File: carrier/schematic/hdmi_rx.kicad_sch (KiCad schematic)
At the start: 7 parts, among them J901 HDMI-019S, U901 M24C02-WMN6TP

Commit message: carrier: wave-2 consolidated regeneration — ALL round-4 gates live (POWER TREE 12 regulators / TESTPOINTS 43+9 / SPICE 14 checks incl. the caught CP2102N abs-max fix), LINK 0/0, goldens 23/23, byte-deterministic
Co-Authored-By: Claude Fable 5 <noreply@anthropic.com>
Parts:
- J901: MPN (none) -> HDMI-019S
- U901: MPN (none) -> M24C02-WMN6TP
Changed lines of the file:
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@@
 		(property
 			"Datasheet"
-			""
+			"https://www.lcsc.com/datasheet/C7562.pdf"
 			(at 113.03 64.77 0)
 			(effects
@@
 			)
 		)
+		(property
+			"MPN"
+			"M24C02-WMN6TP"
+			(at 113.03 64.77 0)
+			(effects
+				(font
+					(size 1.27 1.27)
+				)
+				(hide yes)
+			)
+		)
 		(pin
 			"1"
@@
 				"Zynq_Carrier"
 				(path
-					"/210e47c2-a83b-45be-ae0a-d7b3f3834bfa/3d16c4d5-210e-462e-b61d-a9f0fecc8e09"
+					"/c2797150-7a6e-556a-82f5-fdda13c31368/1e15c56c-3a37-58d2-aa9b-64efface14d2"
 					(reference "U901")
 					(unit 1)
@@
 		(property
 			"Datasheet"
-			""
+			"https://www.lcsc.com/datasheet/C111617.pdf"
 			(at 185.42 90.17 0)
 			(effects
@@
 			)
 		)
+		(property
+			"MPN"
+			"HDMI-019S"
+			(at 185.42 90.17 0)
+			(effects
+				(font
+					(size 1.27 1.27)
+				)
+				(hide yes)
+			)
+		)
 		(pin
 			"16"
@@
 				"Zynq_Carrier"
 				(path
-					"/210e47c2-a83b-45be-ae0a-d7b3f3834bfa/3d16c4d5-210e-462e-b61d-a9f0fecc8e09"
+					"/c2797150-7a6e-556a-82f5-fdda13c31368/1e15c56c-3a37-58d2-aa9b-64efface14d2"
 					(reference "J901")
 					(unit 1)
@@
 				"Zynq_Carrier"
 				(path
-					"/210e47c2-a83b-45be-ae0a-d7b3f3834bfa/3d16c4d5-210e-462e-b61d-a9f0fecc8e09"
+					"/c2797150-7a6e-556a-82f5-fdda13c31368/1e15c56c-3a37-58d2-aa9b-64efface14d2"
 					(reference "R902")
 					(unit 1)
@@
 				"Zynq_Carrier"
 				(path
-					"/210e47c2-a83b-45be-ae0a-d7b3f3834bfa/3d16c4d5-210e-462e-b61d-a9f0fecc8e09"
+					"/c2797150-7a6e-556a-82f5-fdda13c31368/1e15c56c-3a37-58d2-aa9b-64efface14d2"
 					(reference "R901")
 					(unit 1)
@@
 				"Zynq_Carrier"
 				(path
-					"/210e47c2-a83b-45be-ae0a-d7b3f3834bfa/3d16c4d5-210e-462e-b61d-a9f0fecc8e09"
+					"/c2797150-7a6e-556a-82f5-fdda13c31368/1e15c56c-3a37-58d2-aa9b-64efface14d2"
 					(reference "R903")
 					(unit 1)
@@
 				"Zynq_Carrier"
 				(path
-					"/210e47c2-a83b-45be-ae0a-d7b3f3834bfa/3d16c4d5-210e-462e-b61d-a9f0fecc8e09"
+					"/c2797150-7a6e-556a-82f5-fdda13c31368/1e15c56c-3a37-58d2-aa9b-64efface14d2"
 					(reference "R904")
 					(unit 1)
@@
 				"Zynq_Carrier"
 				(path
-					"/210e47c2-a83b-45be-ae0a-d7b3f3834bfa/3d16c4d5-210e-462e-b61d-a9f0fecc8e09"
+					"/c2797150-7a6e-556a-82f5-fdda13c31368/1e15c56c-3a37-58d2-aa9b-64efface14d2"
 					(reference "C901")
 					(unit 1)
@@
 				"Zynq_Carrier"
 				(path
-					"/210e47c2-a83b-45be-ae0a-d7b3f3834bfa/3d16c4d5-210e-462e-b61d-a9f0fecc8e09"
+					"/c2797150-7a6e-556a-82f5-fdda13c31368/1e15c56c-3a37-58d2-aa9b-64efface14d2"
 					(reference "#PWR901")
 					(unit 1)
@@
 				"Zynq_Carrier"
 				(path
-					"/210e47c2-a83b-45be-ae0a-d7b3f3834bfa/3d16c4d5-210e-462e-b61d-a9f0fecc8e09"
+					"/c2797150-7a6e-556a-82f5-fdda13c31368/1e15c56c-3a37-58d2-aa9b-64efface14d2"
 					(reference "#PWR902")
 					(unit 1)
@@
 				"Zynq_Carrier"
 				(path
-					"/210e47c2-a83b-45be-ae0a-d7b3f3834bfa/3d16c4d5-210e-462e-b61d-a9f0fecc8e09"
+					"/c2797150-7a6e-556a-82f5-fdda13c31368/1e15c56c-3a37-58d2-aa9b-64efface14d2"
 					(reference "#PWR903")
 					(unit 1)
@@
 				"Zynq_Carrier"
 				(path
-					"/210e47c2-a83b-45be-ae0a-d7b3f3834bfa/3d16c4d5-210e-462e-b61d-a9f0fecc8e09"
+					"/c2797150-7a6e-556a-82f5-fdda13c31368/1e15c56c-3a37-58d2-aa9b-64efface14d2"
 					(reference "#PWR904")
 					(unit 1)
@@
 				"Zynq_Carrier"
 				(path
-					"/210e47c2-a83b-45be-ae0a-d7b3f3834bfa/3d16c4d5-210e-462e-b61d-a9f0fecc8e09"
+					"/c2797150-7a6e-556a-82f5-fdda13c31368/1e15c56c-3a37-58d2-aa9b-64efface14d2"
 					(reference "#PWR905")
 					(unit 1)
@@
 				"Zynq_Carrier"
 				(path
-					"/210e47c2-a83b-45be-ae0a-d7b3f3834bfa/3d16c4d5-210e-462e-b61d-a9f0fecc8e09"
+					"/c2797150-7a6e-556a-82f5-fdda13c31368/1e15c56c-3a37-58d2-aa9b-64efface14d2"
 					(reference "#PWR906")
 					(unit 1)
@@
 				"Zynq_Carrier"
 				(path
-					"/210e47c2-a83b-45be-ae0a-d7b3f3834bfa/3d16c4d5-210e-462e-b61d-a9f0fecc8e09"
+					"/c2797150-7a6e-556a-82f5-fdda13c31368/1e15c56c-3a37-58d2-aa9b-64efface14d2"
 					(reference "#PWR907")
 					(unit 1)
@@
 				"Zynq_Carrier"
 				(path
-					"/210e47c2-a83b-45be-ae0a-d7b3f3834bfa/3d16c4d5-210e-462e-b61d-a9f0fecc8e09"
+					"/c2797150-7a6e-556a-82f5-fdda13c31368/1e15c56c-3a37-58d2-aa9b-64efface14d2"
 					(reference "#PWR908")
 					(unit 1)
@@
 				"Zynq_Carrier"
 				(path
-					"/210e47c2-a83b-45be-ae0a-d7b3f3834bfa/3d16c4d5-210e-462e-b61d-a9f0fecc8e09"
+					"/c2797150-7a6e-556a-82f5-fdda13c31368/1e15c56c-3a37-58d2-aa9b-64efface14d2"
 					(reference "#FLG901")
 					(unit 1)

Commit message: audit-fix(engine): harvest F1-F7,F9 — gate hardening + leak + guards
F1 selftest now exercises the VISUAL gate against geometry mutants (wire-cross
+ text-over-wire) — proven to bite (was never run on a mutant before).
F2 visual_gate catches different-net wire T-touch / butt-join shorts.
F3 netlist_gate no longer leaks tmp .net files (was 2671 stale).
F4 board uniquify guards the stride (widened 100->1000) against ref collision.
F5 hier-mode sheets now re-run through the per-sheet netlist gate.
F6 dead clause dropped; F7 stale zynq_eda docstring fixed; F9 eager inline-pin
validation. Source copied verbatim from the audit-fix worktree (6 files, proven
untouched on origin since its base); board regenerated fresh. All gates green,
selftest geo-mutants killed by the visual gate, goldens 23/23, m1_rc PASS.

Co-Authored-By: Claude Fable 5 <noreply@anthropic.com>
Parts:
- renumbered C901 to C9001, J901 to J9001, R901 to R9001, R902 to R9002, R903 to R9003, R904 to R9004, U901 to U9001
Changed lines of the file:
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@@
 		(property
 			"Reference"
-			"U901"
+			"U9001"
 			(at 118.11 57.785 0)
 			(effects
@@
 				(path
 					"/c2797150-7a6e-556a-82f5-fdda13c31368/1e15c56c-3a37-58d2-aa9b-64efface14d2"
-					(reference "U901")
+					(reference "U9001")
 					(unit 1)
 				)
@@
 		(property
 			"Reference"
-			"J901"
+			"J9001"
 			(at 200.66 57.785 0)
 			(effects
@@
 				(path
 					"/c2797150-7a6e-556a-82f5-fdda13c31368/1e15c56c-3a37-58d2-aa9b-64efface14d2"
-					(reference "J901")
+					(reference "J9001")
 					(unit 1)
 				)
@@
 		(property
 			"Reference"
-			"R902"
+			"R9002"
 			(at 218.543 128.27 0)
 			(effects
@@
 				(path
 					"/c2797150-7a6e-556a-82f5-fdda13c31368/1e15c56c-3a37-58d2-aa9b-64efface14d2"
-					(reference "R902")
+					(reference "R9002")
 					(unit 1)
 				)
@@
 		(property
 			"Reference"
-			"R901"
+			"R9001"
 			(at 92.608 135.89 0)
 			(effects
@@
 				(path
 					"/c2797150-7a6e-556a-82f5-fdda13c31368/1e15c56c-3a37-58d2-aa9b-64efface14d2"
-					(reference "R901")
+					(reference "R9001")
 					(unit 1)
 				)
@@
 		(property
 			"Reference"
-			"R903"
+			"R9003"
 			(at 87.733 54.61 0)
 			(effects
@@
 				(path
 					"/c2797150-7a6e-556a-82f5-fdda13c31368/1e15c56c-3a37-58d2-aa9b-64efface14d2"
-					(reference "R903")
+					(reference "R9003")
 					(unit 1)
 				)
@@
 		(property
 			"Reference"
-			"R904"
+			"R9004"
 			(at 87.733 62.23 0)
 			(effects
@@
 				(path
 					"/c2797150-7a6e-556a-82f5-fdda13c31368/1e15c56c-3a37-58d2-aa9b-64efface14d2"
-					(reference "R904")
+					(reference "R9004")
 					(unit 1)
 				)
@@
 		(property
 			"Reference"
-			"C901"
+			"C9001"
 			(at 211.939 54.61 0)
 			(effects
@@
 				(path
 					"/c2797150-7a6e-556a-82f5-fdda13c31368/1e15c56c-3a37-58d2-aa9b-64efface14d2"
-					(reference "C901")
+					(reference "C9001")
 					(unit 1)
 				)
@@
 		(property
 			"Reference"
-			"#PWR901"
+			"#PWR9001"
 			(at 99.06 64.77 0)
 			(effects
@@
 				(path
 					"/c2797150-7a6e-556a-82f5-fdda13c31368/1e15c56c-3a37-58d2-aa9b-64efface14d2"
-					(reference "#PWR901")
+					(reference "#PWR9001")
 					(unit 1)
 				)
@@
 		(property
 			"Reference"
-			"#PWR902"
+			"#PWR9002"
 			(at 127 69.85 0)
 			(effects
@@
 				(path
 					"/c2797150-7a6e-556a-82f5-fdda13c31368/1e15c56c-3a37-58d2-aa9b-64efface14d2"
-					(reference "#PWR902")
+					(reference "#PWR9002")
 					(unit 1)
 				)
@@
 		(property
 			"Reference"
-			"#PWR903"
+			"#PWR9003"
 			(at 113.03 72.39 0)
 			(effects
@@
 				(path
 					"/c2797150-7a6e-556a-82f5-fdda13c31368/1e15c56c-3a37-58d2-aa9b-64efface14d2"
-					(reference "#PWR903")
+					(reference "#PWR9003")
 					(unit 1)
 				)
@@
 		(property
 			"Reference"
-			"#PWR904"
+			"#PWR9004"
 			(at 193.04 123.19 0)
 			(effects
@@
 				(path
 					"/c2797150-7a6e-556a-82f5-fdda13c31368/1e15c56c-3a37-58d2-aa9b-64efface14d2"
-					(reference "#PWR904")
+					(reference "#PWR9004")
 					(unit 1)
 				)
@@
 		(property
 			"Reference"
-			"#PWR905"
+			"#PWR9005"
 			(at 205.74 123.19 0)
 			(effects
@@
 				(path
 					"/c2797150-7a6e-556a-82f5-fdda13c31368/1e15c56c-3a37-58d2-aa9b-64efface14d2"
-					(reference "#PWR905")
+					(reference "#PWR9005")
 					(unit 1)
 				)
@@
 		(property
 			"Reference"
-			"#PWR906"
+			"#PWR9006"
 			(at 215.9 123.19 0)
 			(effects
@@
 				(path
 					"/c2797150-7a6e-556a-82f5-fdda13c31368/1e15c56c-3a37-58d2-aa9b-64efface14d2"
-					(reference "#PWR906")
+					(reference "#PWR9006")
 					(unit 1)
 				)
@@
 		(property
 			"Reference"
-			"#PWR907"
+			"#PWR9007"
 			(at 85.09 67.31 0)
 			(effects
@@
 				(path
 					"/c2797150-7a6e-556a-82f5-fdda13c31368/1e15c56c-3a37-58d2-aa9b-64efface14d2"
-					(reference "#PWR907")
+					(reference "#PWR9007")
 					(unit 1)
 				)
@@
 		(property
 			"Reference"
-			"#PWR908"
+			"#PWR9008"
 			(at 208.28 57.15 0)
 			(effects
@@
 				(path
 					"/c2797150-7a6e-556a-82f5-fdda13c31368/1e15c56c-3a37-58d2-aa9b-64efface14d2"
-					(reference "#PWR908")
+					(reference "#PWR9008")
 					(unit 1)
 				)
@@
 		(property
 			"Reference"
-			"#FLG901"
+			"#FLG9001"
 			(at 151.13 46.99 0)
 			(effects
@@
 				(path
 					"/c2797150-7a6e-556a-82f5-fdda13c31368/1e15c56c-3a37-58d2-aa9b-64efface14d2"
-					(reference "#FLG901")
-					(unit 1)
-				)
+					(reference "#FLG9001")
+					(unit 1)
+				)

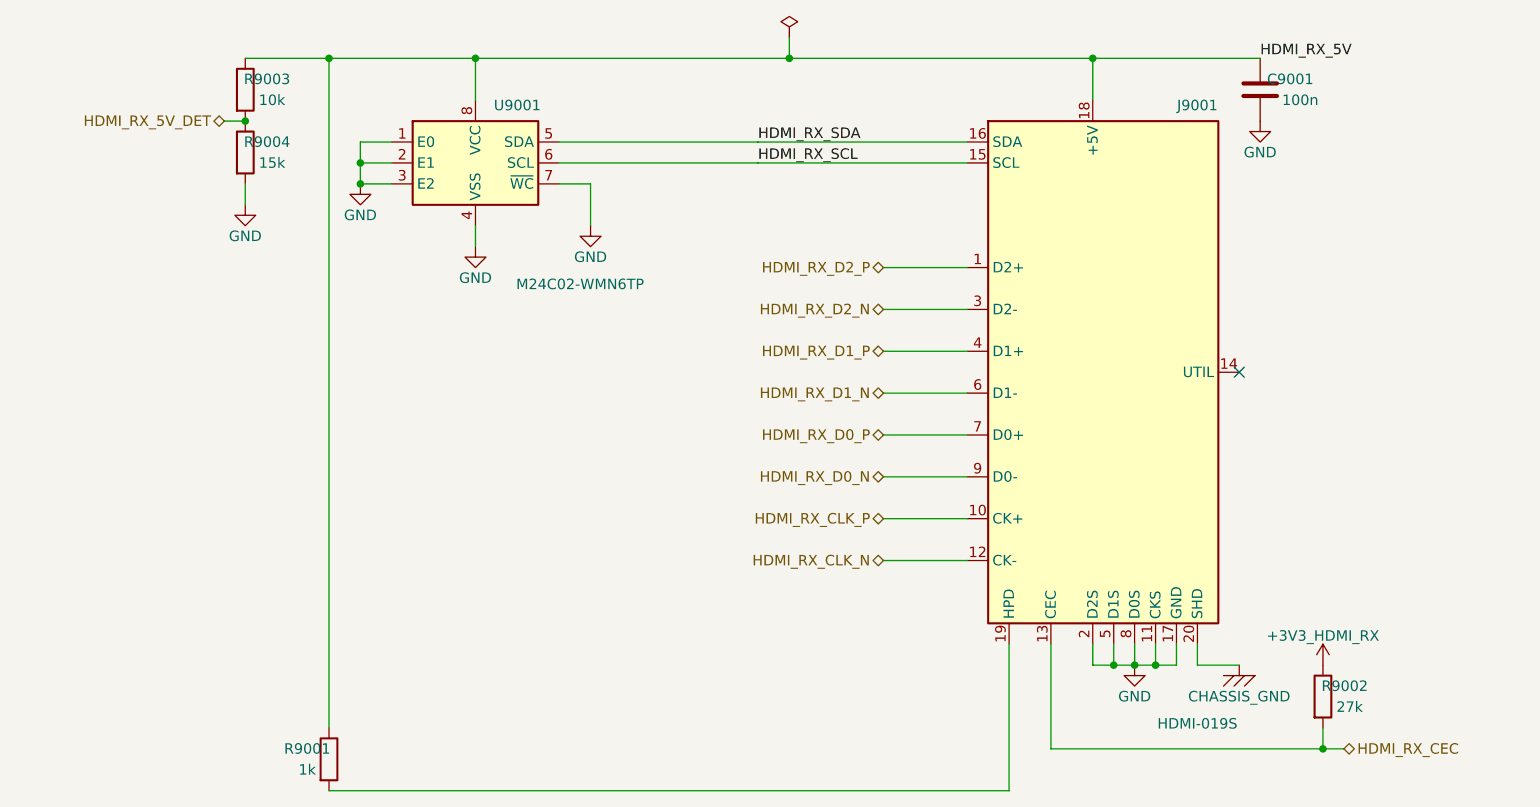
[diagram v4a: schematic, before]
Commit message: carrier: consolidated regen for round-6 audit fixes + PLAN RESOLVED
schgen board regen after SD-1 / HDMIRX-1 / HDMIRX-2 / LCD-1: 23 sheets, all
gates green (board-link, ERC=0, power-tree 16 regs/0 findings, testpoints,
SPICE 21 checks, visual). Goldens drift only on the 3 touched sheets
(microsd/hdmi_rx/lcd schematic+render), BOM (microsd:C4 100n, hdmi_rx:R5 10k,
lcd:C2 2.2u/C125847), reports, floorplan. PLAN findings marked RESOLVED
(HDMIRX-1 = documented verified-part DNP). selftest 44/44 + byte-deterministic.

Co-Authored-By: Claude Fable 5 <noreply@anthropic.com>
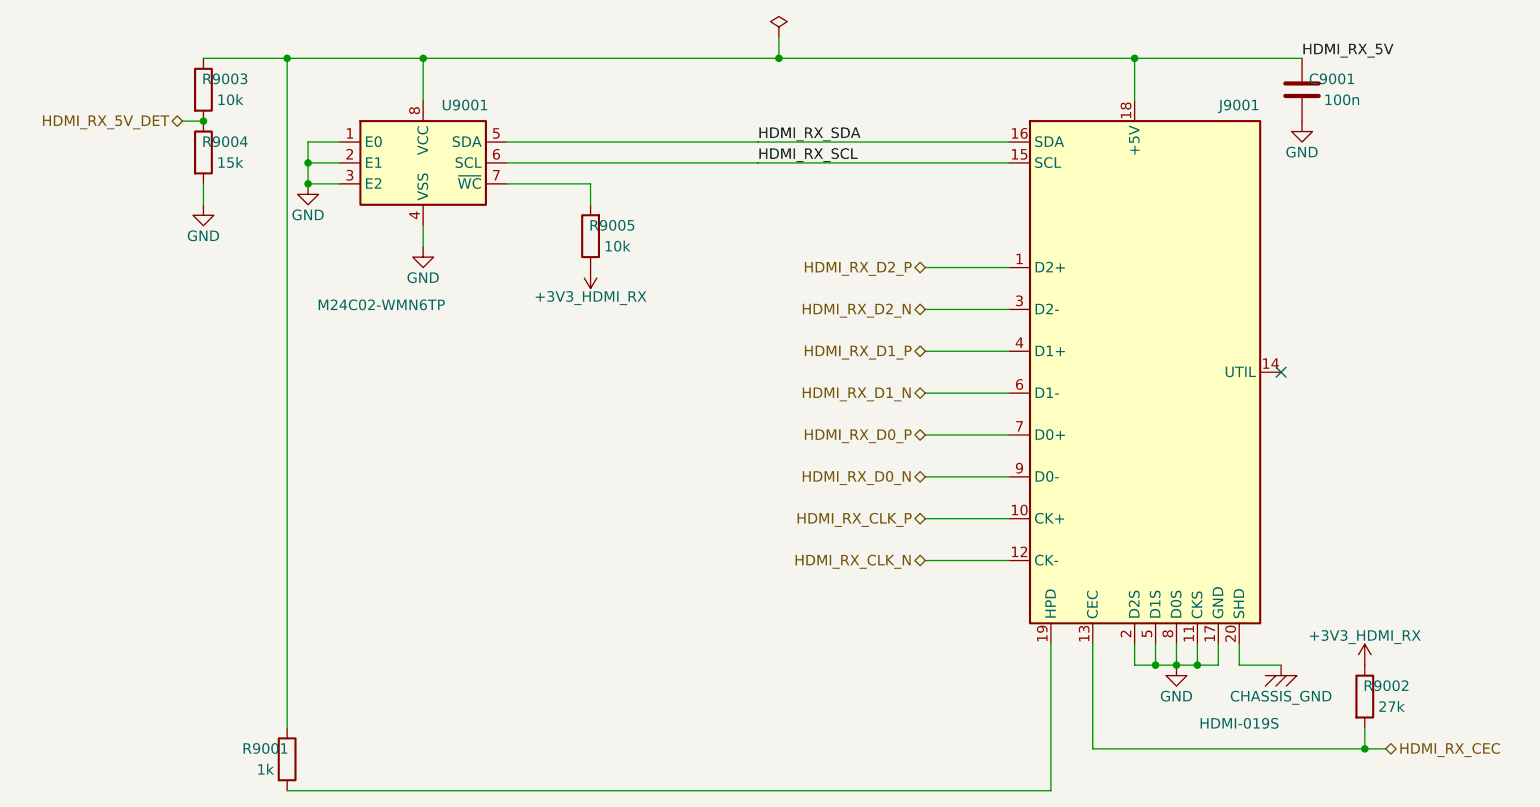
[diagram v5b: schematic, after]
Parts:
- added C9001: 100n, Capacitor_SMD:C_0603_1608Metric, symbol Device:C
- J9001: renamed from R9002; value 27k -> HDMI-019S; footprint Resistor_SMD:R_0603_1608Metric -> HDMI-019S:HDMI-019S; symbol Device:R -> schgen:HDMI_A_RX; LCSC C22967 -> C111617; MPN (none) -> HDMI-019S
- R9001: renamed from R9003; value 10k -> 1k; LCSC C25804 -> C21190
- R9002: renamed from R9001; value 1k -> 27k; LCSC C21190 -> C22967
- R9003: renamed from R9004; value 15k -> 10k; LCSC C22809 -> C25804
- R9004: renamed from C9001; value 100n -> 15k; footprint Capacitor_SMD:C_0603_1608Metric -> Resistor_SMD:R_0603_1608Metric; symbol Device:C -> Device:R; LCSC C14663 -> C22809
- R9005: renamed from J9001; value HDMI-019S -> 10k; footprint HDMI-019S:HDMI-019S -> Resistor_SMD:R_0603_1608Metric; symbol schgen:HDMI_A_RX -> Device:R; LCSC C111617 -> C25804; MPN HDMI-019S -> (none)
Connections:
- net +3V3_HDMI_RX: now also R9002.1, R9005.1; no longer J9001.1
- net CHASSIS_GND: now also J9001.20 (SHD), J9001.21 (SHD), J9001.22 (SHD), J9001.23 (SHD); no longer R9005.20 (SHD), R9005.21 (SHD), R9005.22 (SHD), R9005.23 (SHD)
- net GND: now also J9001.11 (CKS), J9001.17 (GND), J9001.2 (D2S), J9001.5 (D1S), J9001.8 (D0S), C9001.2; no longer R9003.2, R9005.11 (CKS), R9005.17 (GND), R9005.2 (D2S), R9005.5 (D1S), R9005.8 (D0S), U9001.7 (~{WC})
- net HDMI_RX_5V: now also J9001.18 (+5V), R9003.1, C9001.1; no longer R9002.1, R9004.1, R9005.18 (+5V)
- net HDMI_RX_5V_DET: now also R9003.2, R9004.1; no longer R9001.2, R9003.1
- net HDMI_RX_CEC: now also J9001.13 (CEC), R9002.2; no longer J9001.2, R9005.13 (CEC)
- net HDMI_RX_CLK_N: now also J9001.12 (CK-); no longer R9005.12 (CK-)
- net HDMI_RX_CLK_P: now also J9001.10 (CK+); no longer R9005.10 (CK+)
- net HDMI_RX_D0_N: now also J9001.9 (D0-); no longer R9005.9 (D0-)
- net HDMI_RX_D0_P: now also J9001.7 (D0+); no longer R9005.7 (D0+)
- net HDMI_RX_D1_N: now also J9001.6 (D1-); no longer R9005.6 (D1-)
- net HDMI_RX_D1_P: now also J9001.4 (D1+); no longer R9005.4 (D1+)
- net HDMI_RX_D2_N: now also J9001.3 (D2-); no longer R9005.3 (D2-)
- net HDMI_RX_D2_P: now also J9001.1 (D2+); no longer R9005.1 (D2+)
- net HDMI_RX_SCL: now also J9001.15 (SCL); no longer R9005.15 (SCL)
- net HDMI_RX_SDA: now also J9001.16 (SDA); no longer R9005.16 (SDA)
- new net: J9001.19 (HPD), R9001.2
- new net: R9005.2, U9001.7 (~{WC})
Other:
- moved on the sheet: R9001, R9002, R9003, U9001
